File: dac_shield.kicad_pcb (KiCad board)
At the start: 2 copper layers, 68.6 x 53.3 mm, 32 parts, among them P1 CONN_2, P2 CONN_2, P3 CONN_2, T1 VrefTest, U1 MCP4921, U2 TCA0372, U3 LM741

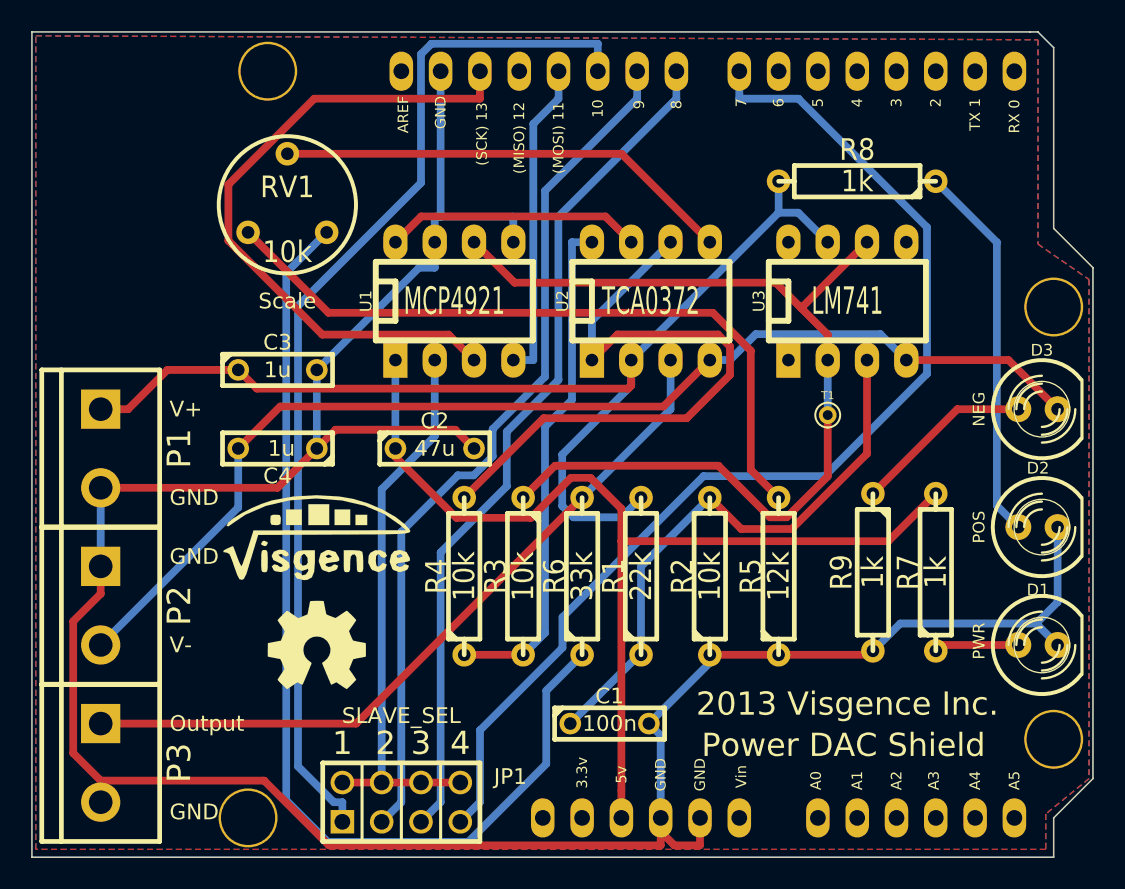
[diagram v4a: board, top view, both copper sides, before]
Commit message: Changed resistors and caps to SMD
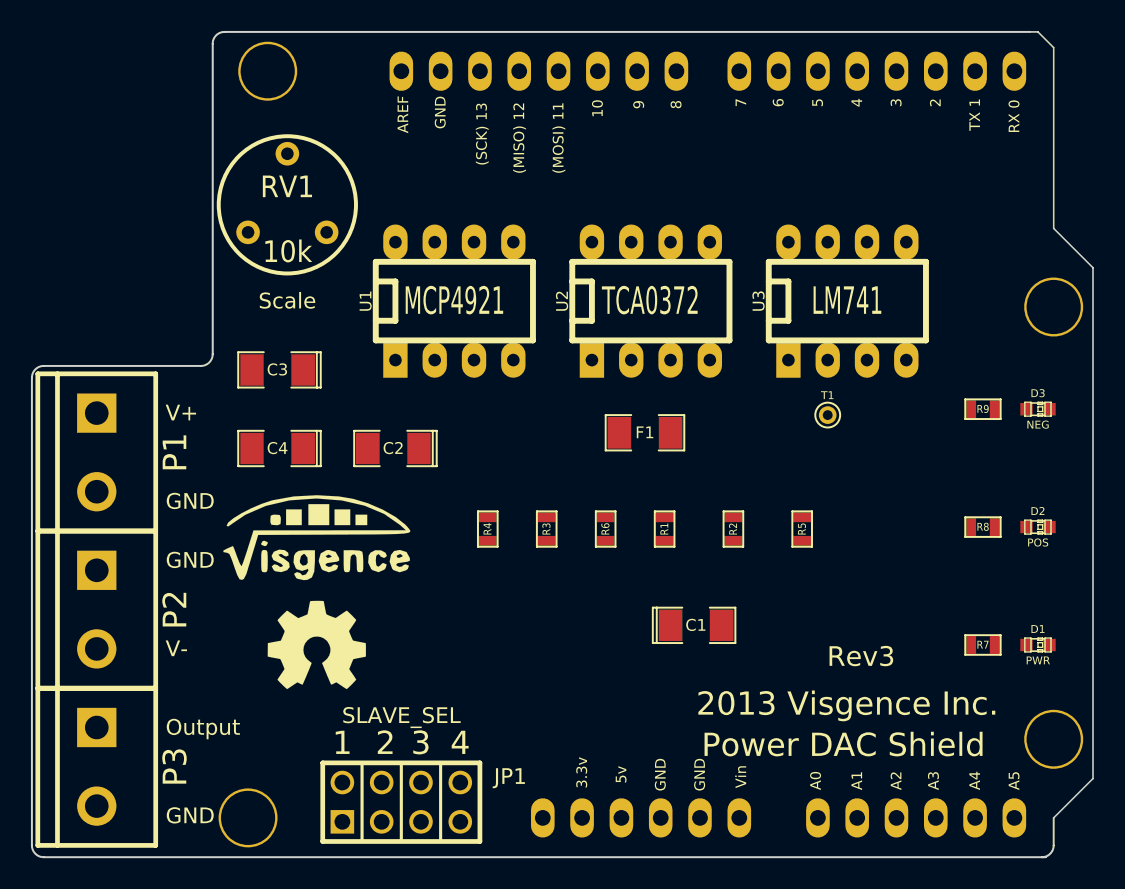
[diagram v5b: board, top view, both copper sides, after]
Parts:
- added F1: FUSE, SM1206, F.Cu at (70.1, 54.9)
- C1, C2, C3, C4: footprint C2 -> SM1206POL
- D1, D2, D3: footprint LED-5MM -> LED-0603
- R1, R2, R3, R4, R5, R6, R7, R8, R9: footprint R4 -> SM0603
- moved R8 23.8 mm to (91.9, 61.0)
- moved R9 12.7 mm to (91.9, 53.3), turned to 180 degrees
- moved C1 8.46 mm to (73.4, 67.3)
- moved R7 5.60 mm to (91.9, 68.6), turned to 180 degrees
- moved R1 3.41 mm to (71.4, 61.1)
- moved R2 3.41 mm to (75.8, 61.1)
- moved R3 3.41 mm to (63.8, 61.1)
- moved R4 3.41 mm to (59.9, 61.1)
- moved R5 3.41 mm to (80.3, 61.1)
- moved R6 3.41 mm to (67.6, 61.1)
- moved C2 2.67 mm to (53.8, 55.9), turned to 180 degrees
- moved P1 0.36 mm to (34.7, 56.1)
- moved P2 0.36 mm to (34.7, 66.3)
- moved P3 0.36 mm to (34.7, 76.5)
- turned C3 to 180 degrees
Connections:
- R6 pad 2: N-000009 -> N-000007
- U2 pad 3: N-000009 -> N-000007
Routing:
- net GND: track 170.4 -> 0.00 mm
- net VSS: track 74.4 -> 0.00 mm
- net VDD: track 74.2 -> 0.00 mm
- net N-0000034: track 72.9 -> 0.00 mm
- net N-0000036: track 67.9 -> 0.00 mm
- net +5V: track 66.0 -> 0.00 mm
- net N-0000041: track 65.8 -> 0.00 mm
- net VREF: track 63.5 -> 0.00 mm
- net N-0000033: track 55.9 -> 0.00 mm
- net N-0000035: track 55.4 -> 0.00 mm
- net N-000009: track 48.4 -> 0.00 mm
- net N-0000040: track 45.9 -> 0.00 mm
- net CLK: track 43.0 -> 0.00 mm
- net N-0000043: track 42.0 -> 0.00 mm
- net N-000006: track 37.5 -> 0.00 mm
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- removed copper zone on B.Cu, net GND
- removed copper zone on F.Cu, net GND
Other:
- outline, holes or cut-outs redrawn
- board text added: "Rev3"
